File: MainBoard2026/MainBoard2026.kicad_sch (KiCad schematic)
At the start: 52 parts, among them J1 RJ25, J2 RJ25, J3 BATT_CON, J4 PRG_TWE, J5 GPS_DFROBOT_TEL-0157, J6 Micro_SD_Card_Det_Hirose_DM3AT, J7 RJ25, Q1 AO3401A, SW2 POWER, SW3 SW_Push, SW4 REG, U2 R-78E5.0-0.5, U3 MCP25625-x-SS, U4 Pico2W, U6 RX8900_mod, U7 TWE-L-WX, U8 IM920sl, Y1 16MHz

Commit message: Add files via upload
Raspberry Pi Pico W からESP32に変更　2025.09.17
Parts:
- removed D9: IM920, LED_SMD:LED_0603_1608Metric, symbol Device:LED
- removed J4: PRG_TWE, Connector_PinSocket_2.54mm:PinSocket_1x06_P2.54mm_Vertical, symbol Connector:Conn_01x06_Socket
- removed J7: RJ25, Connector_RJ:RJ25_Wayconn_MJEA-660X1_Horizontal, symbol Connector:RJ25
- removed JP2: M1, Jumper:SolderJumper-2_P1.3mm_Open_RoundedPad1.0x1.5mm, symbol Jumper:SolderJumper_2_Open
- removed JP3: BPS, Jumper:SolderJumper-2_P1.3mm_Open_RoundedPad1.0x1.5mm, symbol Jumper:SolderJumper_2_Open
- removed JP4: TX, Connector_PinHeader_2.54mm:PinHeader_1x02_P2.54mm_Vertical, symbol Jumper:SolderJumper_2_Open
- removed JP5: RX, Connector_PinHeader_2.54mm:PinHeader_1x02_P2.54mm_Vertical, symbol Jumper:SolderJumper_2_Open
- removed R12: 1k, Resistor_SMD:R_0603_1608Metric, symbol Device:R_US
- removed SW3: SW_Push, Button_Switch_SMD:SW_SPST_PTS810, symbol Switch:SW_Push
- removed SW4: REG, Button_Switch_SMD:SW_SPST_PTS810, symbol Switch:SW_Push
- removed U4: Pico2W, RPi_Pico:RPi_PicoW_SMD_TH, symbol RPi_Pico:PicoW
- removed U7: TWE-L-WX, RF_Module:MonoWireless_TWE-L-WX, symbol RF_ZigBee:TWE-L-WX
- removed U8: IM920sl, KUBTSS_parts:IM920c_ADP, symbol AKI_PARTS:IM920-DIP
- added C1, C12, C8: 0.1u, Capacitor_SMD:C_0603_1608Metric, symbol Device:C
- added C10, C11, C5: 10u, Capacitor_SMD:C_1206_3216Metric, symbol Device:C
- added C9: 1000p, Capacitor_SMD:C_0603_1608Metric, symbol Device:C
- added D11, D12: RB160M, Diode_SMD:D_SOD-123, symbol Device:D_Schottky
- added J7: USB_C_Receptacle_USB2.0_14P, Connector_USB:USB_C_Receptacle_HRO_TYPE-C-31-M-12, symbol Connector:USB_C_Receptacle_USB2.0_14P
- added Q2, Q3: MMBT3904, Package_TO_SOT_SMD:SOT-23, symbol Transistor_BJT:MMBT3904
- added R13, R14, R15, R16: 10k, Resistor_SMD:R_0603_1608Metric, symbol Device:R_US
- added R17, R18: 5.1k, Resistor_SMD:R_0603_1608Metric, symbol Device:R_US
- added SW1: RST, Button_Switch_SMD:SW_SPST_PTS810, symbol Switch:SW_Push
- added SW5: BOOT, Button_Switch_SMD:SW_SPST_PTS810, symbol Switch:SW_Push
- added U1: ESP32-WROOM-32, RF_Module:ESP32-WROOM-32, symbol RF_Module:ESP32-WROOM-32
- added U10: CH340G, Package_SO:SOIC-16_3.9x9.9mm_P1.27mm, symbol Interface_USB:CH340G
- added U9: LM1117MP-3.3, Package_TO_SOT_SMD:SOT-223-3_TabPin2, symbol Regulator_Linear:LM1117MP-3.3
- added Y2: 12MHz, Crystal:Resonator_SMD_Murata_CSTxExxV-3Pin_3.0x1.1mm, symbol Device:Resonator_Small
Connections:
- net +3V3: now also J5.1 (Pin_1), C11.1, C12.1, C5.1, C8.1, D12.2 (A), R13.1, R14.1, U1.2 (VDD), U10.16 (VCC), U10.4 (V3), U9.2 (VO)
- net +5V: no longer J5.1 (Pin_1)
- net BAT: now also U1.6 (IO34)
- net CS: now also U1.9 (IO33)
- net ERR: now also U1.7 (IO35)
- net GND: now also C1.2, C10.2, C11.2, C12.2, C5.2, C8.2, C9.2, J7.A1 (GND), J7.A12 (GND), J7.B1 (GND), J7.B12 (GND), J7.S1 (SHIELD), R17.2, R18.1, SW1.1, SW5.2, U1.1 (GND), U1.15 (GND), U1.38 (GND), U1.39 (GND), U10.1 (GND), U9.1 (GND), Y2.2
- net INT: now also U1.8 (IO32)
- net RX1: now also U1.34 (RXD0/IO3)
- net SCL: now also U1.13 (IO14)
- net SDA: now also U1.23 (IO15)
- net TX1: now also U1.35 (TXD0/IO1)
- net VSENS: now also U1.29 (IO5)
- new net: D11.2 (A), J7.A4 (VBUS), J7.A9 (VBUS), J7.B4 (VBUS), J7.B9 (VBUS)
- new net: J7.A5 (CC1), R17.1
- new net: J7.A6 (D+), J7.B6 (D+), U10.5 (UD+)
- new net: J7.A7 (D-), J7.B7 (D-), U10.6 (UD-)
- new net: J7.B5 (CC2), R18.2
- new net: Q3.1 (B), R16.2
- new net: Q2.1 (B), R15.2
- new net: C10.1, D11.1 (K), D12.1 (K), U9.3 (VI)
- new net: U10.7 (XI), Y2.1
- new net: U10.8 (XO), Y2.3
- new net DTR: Q2.2 (E), R16.1, U10.13 (~{DTR})
- new net EN: C1.1, Q2.3 (C), R13.2, SW1.2, U1.3 (EN)
- new net IO0: C9.1, Q3.3 (C), R14.2, SW5.1, U1.25 (IO0)
- new net RTS: Q3.2 (E), R15.1, U10.14 (~{RTS})
- new net RX: U1.16 (IO13), U10.2 (TXD)
- new net TX: U1.14 (IO12), U10.3 (RXD)
- no-connect marks 65 -> 25
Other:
- note added: "INPUT OUTPUT DTR RTS EN IO0 1 1 1 1 0 0 1 1 1 0 0 1 0 1 1 0"
- note removed: "Raspberry pi picoにBLE:Bluetooth Low Energyが対応している スマホとの接続、ログの管理"
- note removed: "tweliteのライターを指すためのソケット"
- note removed: "こっちのジャンパーはハンダを使うので小さい、どちらの面にあっても良い"
- note removed: "こっちはジャンパーケーブルで繋ぐ(そうすると多分ラク)ので背がある"
- note removed: "・ラズパイピコ２だけで制御と通信の両方を行えるのか ・IM920より小さい通信機でもいいな"
- moved on the sheet: C2, C3, C4, C6, D8, J6, R11, R3, U3, Y1

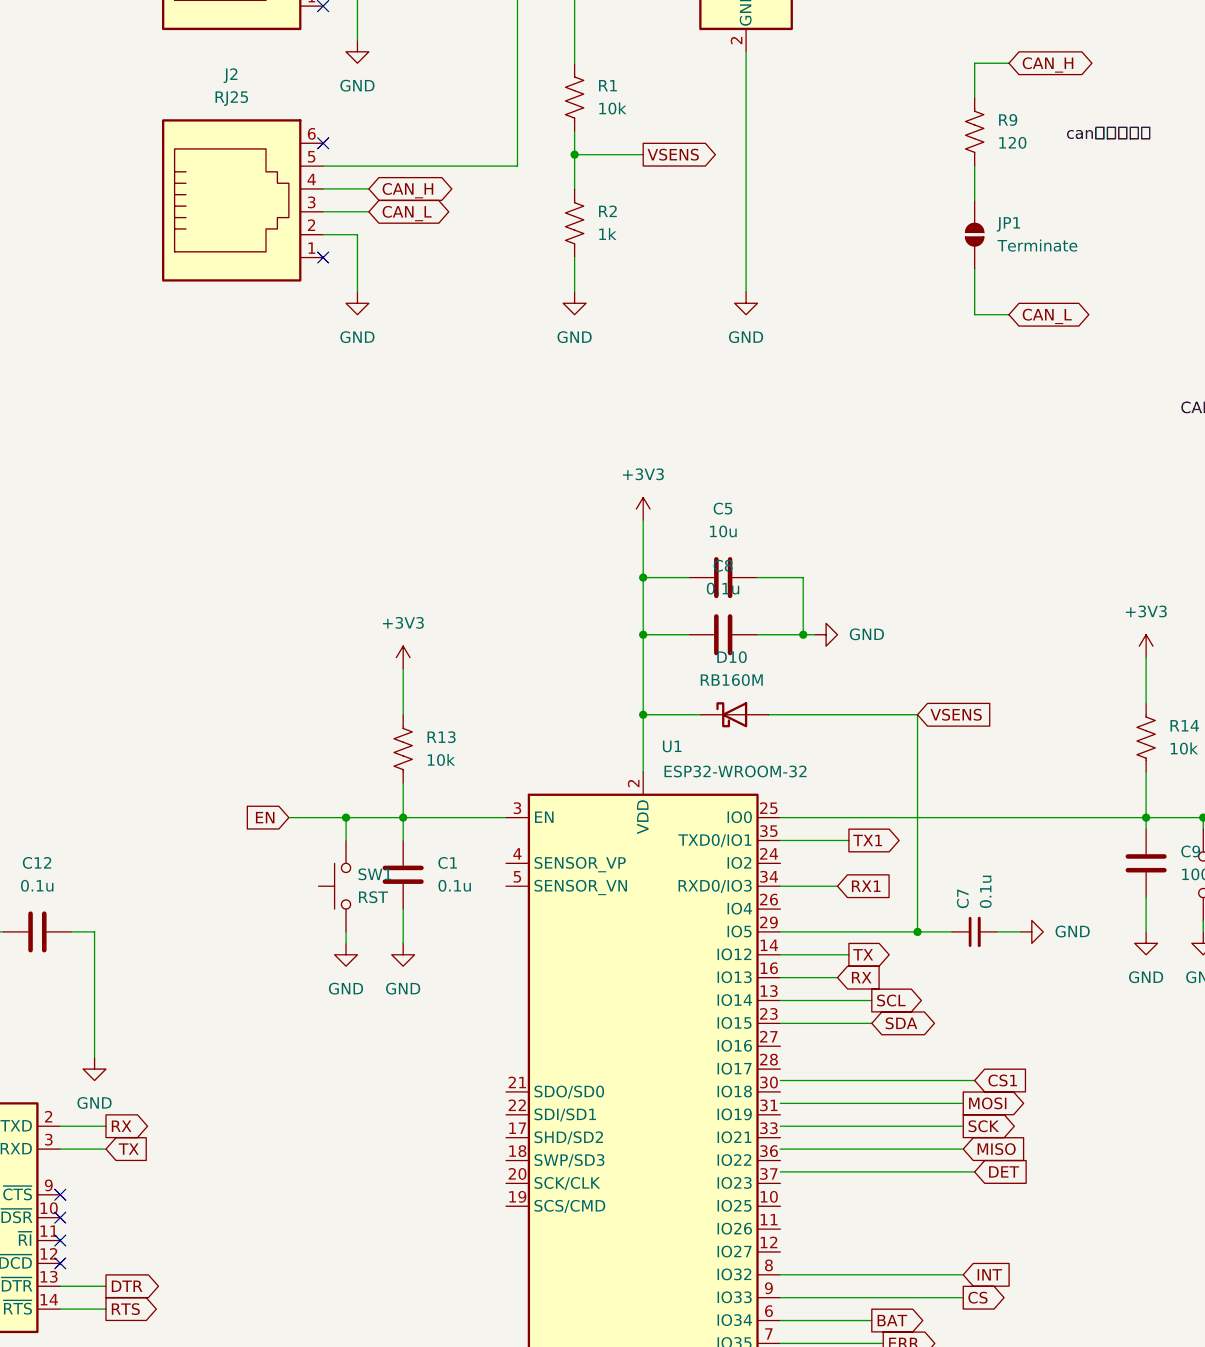
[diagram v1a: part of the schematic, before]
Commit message: Add files via upload
CANコネクタを増やした
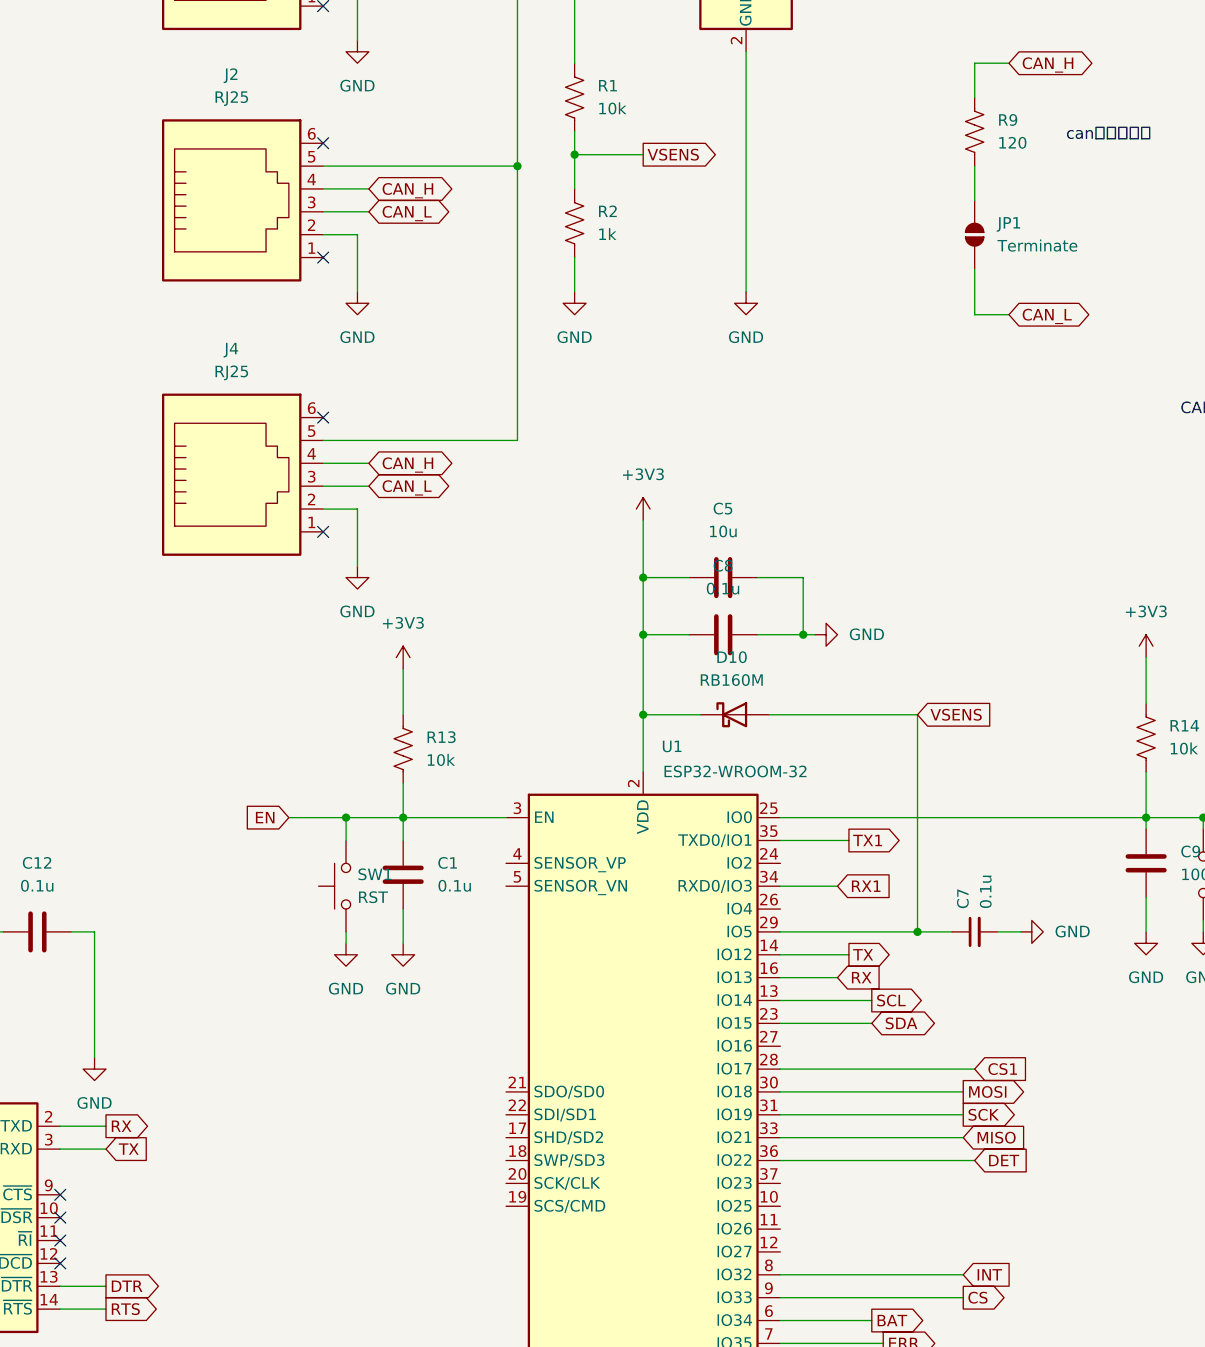
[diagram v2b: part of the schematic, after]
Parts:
- added J4: RJ25, Connector_RJ:RJ25_Wayconn_MJEA-660X1_Horizontal, symbol Connector:RJ25
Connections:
- net +BATT: now also J4.5
- net CAN_H: now also J4.4
- net CAN_L: now also J4.3
- net CS1: now also U1.28 (IO17)
- net DET: now also U1.36 (IO22)
- net GND: now also J4.2
- net MISO: now also U1.33 (IO21)
- net MOSI: now also U1.30 (IO18)
- net SCK: now also U1.31 (IO19)
- no-connect marks 25 -> 27

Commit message: Add files via upload
試作前完成版
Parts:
- removed D2: Zener_12V, Diode_SMD:D_SOD-323, symbol Device:D_Zener
- removed D3: MA10EB045, Diode_SMD:Vishay_SMPA, symbol Device:D_Schottky
- removed J3: BATT_CON, Connector_AMASS:AMASS_XT60PW-M_1x02_P7.20mm_Horizontal, symbol Connector_Generic:Conn_01x02
- removed Q1: AO3401A, Package_TO_SOT_SMD:SOT-23, symbol Device:Q_PMOS_GDS
- removed R4: 10k, Resistor_SMD:R_0603_1608Metric, symbol Device:R_US
- removed R8: 100, Resistor_SMD:R_0603_1608Metric, symbol Device:R_US
- removed SW2: POWER, KUBTSS:toggle, symbol Switch:SW_SPDT
- added C13: 10u, Capacitor_SMD:C_0603_1608Metric, symbol Device:C_Small
- added C14, C16, C21, C23, C24, C27, C28: 0.1u, Capacitor_SMD:C_0603_1608Metric, symbol Device:C_Small
- added C15: 1u, Capacitor_SMD:C_0603_1608Metric, symbol Device:C_Small
- added C17: 100u, Capacitor_SMD:C_1206_3216Metric, symbol Device:C
- added C18: 1n, Capacitor_SMD:C_1206_3216Metric, symbol Device:C
- added C19, C20: 0.1u, Capacitor_SMD:C_0603_1608Metric, symbol Device:C
- added C22, C25, C26, C29: 22u, Capacitor_SMD:C_0603_1608Metric, symbol Device:C_Small
- added D20: Zener_10V, Diode_SMD:D_SOD-323, symbol Device:D_Zener
- added D9: RB160M, Diode_SMD:D_SOD-123, symbol Device:D_Schottky
- added F1, F2: Fuse, symbol Device:Fuse
- added FB1: FerriteBead_Small, symbol Device:FerriteBead_Small
- added J8: BATT_CON, Connector_AMASS:AMASS_XT60PW-M_1x02_P7.20mm_Horizontal, symbol Connector_Generic:Conn_01x02
- added Q4: AO3401A, Package_TO_SOT_SMD:SOT-23, symbol Device:Q_PMOS_GDS
- added R12, R19, R23, R25, R27, R42: 100k, Resistor_SMD:R_0603_1608Metric, symbol Device:R_US
- added R20, R21, R22: 47, Resistor_SMD:R_0603_1608Metric, symbol Device:R_US
- added R24, R40, R44: 100, Resistor_SMD:R_0603_1608Metric, symbol Device:R_US
- added R26: 200k, Resistor_SMD:R_0603_1608Metric, symbol Device:R_US
- added R28, R29: 2.2k, Resistor_SMD:R_0603_1608Metric, symbol Device:R_US
- added R30, R31, R32, R33: 33, Resistor_SMD:R_0603_1608Metric, symbol Device:R_US
- added R34, R35: 0.3, Resistor_SMD:R_0603_1608Metric, symbol Device:R_US
- added R36, R37: 22, Resistor_SMD:R_0603_1608Metric, symbol Device:R_US
- added R38: 3.3k, Resistor_SMD:R_0603_1608Metric, symbol Device:R_US
- added R39: 6.8k, Resistor_SMD:R_0603_1608Metric, symbol Device:R_US
- added R41: 1M, Resistor_SMD:R_0603_1608Metric, symbol Device:R_US
- added SW3: POWER, KUBTSS:toggle, symbol Switch:SW_SPDT
- added U4: R-78E3.3-0.5, Converter_DCDC:Converter_DCDC_RECOM_R-78E-0.5_THT, symbol Regulator_Switching:R-78E5.0-0.5
- C1: value 0.1u -> 0.47u
- C2: value 0.1u -> 10u
- C3: value 0.1u -> 1u
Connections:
- net +3V3: now also C13.2, C15.1, C16.1, C17.1, R12.2, R19.2, R28.1, R29.1; no longer C2.2, C3.1, U10.16 (VCC), U10.4 (V3), U3.19 (VDD)
- net +5V: now also C3.1, U3.19 (VDD), C14.1, C22.2, C23.2, FB1.1; no longer C4.1, U3.27 (VDDA)
- net +BATT: now also C24.2, C25.2, C26.2, C27.2, D9.1 (K), Q4.2 (D), U4.1 (IN)
- net CS1: now also R21.1, R30.2; no longer J6.2 (DAT3/CD), U1.28 (IO17)
- net GND: now also C2.2, J6.11 (SHIELD), C13.1, C14.2, C15.2, C16.2, C17.2, C18.2, C19.2, C22.1, C23.1, C24.1, C25.1, C26.1, C27.1, C28.1, C29.1, J8.1 (Pin_1), R23.2, R25.2, R34.2, R35.1, R39.2, R41.2, SW3.1 (A), U4.2 (GND); no longer C10.2, C11.2, C2.1, J7.S1 (SHIELD), U3.5 (STBY)
- net IO0: now also R24.2; no longer U1.25 (IO0)
- net MISO: now also R33.2; no longer U1.33 (IO21)
- net MOSI: now also R22.1, R31.2; no longer J6.3 (CMD), U1.30 (IO18)
- net RX: now also R38.1, R39.1; no longer U10.2 (TXD)
- net SCK: now also R20.1, R32.2; no longer D4.2 (A), D8.2 (A), J6.5 (CLK), U1.31 (IO19)
- net SCL: now also R28.2
- net SDA: now also R29.2
- net TX: now also R25.1, R40.1; no longer U10.3 (RXD)
- net VSENS: now also R26.2, R27.1; no longer C7.1, D10.2 (A), U1.29 (IO5)
- net at J7.A4 (VBUS), J7.A9 (VBUS), J7.B4 (VBUS)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: now also F1.2; no longer D11.2 (A)
- net at J7.A6 (D+), J7.B6 (D+): now also R37.2; no longer U10.5 (UD+)
- net at J7.A7 (D-), J7.B7 (D-): now also R36.2; no longer U10.6 (UD-)
- net at C10.1, D11.1 (K), D12.1 (K)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: now also C20.1
- net LED1: now reaches U1.10 (IO25)
- net LED1: now also D4.2 (A)
- net LED2: now reaches U1.11 (IO26)
- net LED2: now also D8.2 (A)
- net at J6.1 (DAT2): now also J6.8 (DAT1), R19.1
- new net: R24.1, U1.25 (IO0)
- new net: J6.2 (DAT3/CD), R12.1, R21.2
- new net: R36.1, U10.6 (UD-)
- new net: C18.1, J7.S1 (SHIELD), R41.1
- new net: R23.1, U3.5 (STBY)
- new net: R42.1, R44.1, SW3.2 (B)
- new net: C21.2, D20.1 (K), F2.2, Q4.3 (S), R42.2, SW3.3 (C)
- new net: C7.1, R27.2, U1.29 (IO5)
- new net: R40.2, U10.3 (RXD)
- new net: C11.2, R35.2
- new net: C10.2, R34.1
- new net: R37.1, U10.5 (UD+)
- new net: C2.1, C4.1, FB1.2, U3.27 (VDDA)
- new net: C19.1, U10.4 (V3)
- new net: C21.1, D20.2 (A), Q4.1 (G), R44.2
- new net: J6.3 (CMD), R22.2
- new net: R31.1, U1.30 (IO18)
- new net: J6.5 (CLK), R20.2
- new net: D10.2 (A), R26.1
- new net: R30.1, U1.28 (IO17)
- new net: R32.1, U1.31 (IO19)
- new net: R33.1, U1.33 (IO21)
- new net: F2.1, J8.2 (Pin_2)
- new net: C20.2, U10.16 (VCC)
- new net: R38.2, U10.2 (TXD)
- new net: D11.2 (A), F1.1
- new net +3.3V: C28.2, C29.2, D9.2 (A), U4.3 (OUT)
- no-connect marks 27 -> 24
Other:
- note added: "D"
- note added: "G"
- note added: "S"
- note added: "VDD近くに配置"
- moved on the sheet: C1, C10, C11, C12, C3, C4, C5, C6, C7, C8, C9, D1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

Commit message: Add files via upload
試作後　抵抗値など修正　2025.10.25
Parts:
- removed R22: 47, Resistor_SMD:R_0603_1608Metric, symbol Device:R_US
- removed R33: 33, Resistor_SMD:R_0603_1608Metric, symbol Device:R_US
- added R4: 100k, Resistor_SMD:R_0603_1608Metric, symbol Device:R_US
- added R8: 22, Resistor_SMD:R_0603_1608Metric, symbol Device:R_US
- C21: value 0.1u -> 1u
- R12: value 100k -> 47k
- R20: value 47 -> 22
- R21: value 47 -> 33
- R44: value 100 -> 4.7k
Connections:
- net +3V3: now also R4.1
- net +BATT: no longer Q4.2 (D)
- net CS: now also R20.2, R21.1; no longer U1.9 (IO33), U3.17 (~{CS})
- net CS1: now also J6.2 (DAT3/CD), R12.1; no longer R21.1
- net GND: now also C20.1
- net MISO: now also U1.33 (IO21), R8.2; no longer J6.7 (DAT0)
- net MOSI: now also J6.3 (CMD), R4.2
- net RX: now also U1.34 (RXD0/IO3); no longer U1.16 (IO13)
- net RX1: now also U1.16 (IO13); no longer U1.34 (RXD0/IO3)
- net SCK: now also J6.5 (CLK); no longer R20.1
- net TX: now also U1.35 (TXD0/IO1); no longer R25.1, U1.14 (IO12)
- net TX1: now also R25.1, U1.14 (IO12); no longer U1.35 (TXD0/IO1)
- net at C10.1, D11.1 (K), D12.1 (K)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: now also C20.2, U10.16 (VCC); no longer C20.1
- new net: R20.1, U3.17 (~{CS})
- new net: R21.2, U1.9 (IO33)
- new net: J6.7 (DAT0), R8.1
- new net +out: Q4.2 (D)
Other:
- note added: "SdFat.h"
- moved on the sheet: C10, C11, C12, C18, C19, C20, D11, D12, F1, J7, Q2, Q3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

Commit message: Add files via upload
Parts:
- removed R28, R29: 2.2k, Resistor_SMD:R_0603_1608Metric, symbol Device:R_US
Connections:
- net +3V3: no longer J5.1 (Pin_1)
- net +5V: now also J5.1 (Pin_1)
- net RX1: now also U1.27 (IO16); no longer U1.16 (IO13)
- net TX1: now also U1.12 (IO27); no longer R25.1, U1.14 (IO12)
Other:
- moved on the sheet: R25

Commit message: Add files via upload
フットプリント設定完了
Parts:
- removed C1: 0.47u, Capacitor_SMD:C_0603_1608Metric, symbol Device:C
- removed C10, C11: 10u, Capacitor_SMD:C_1206_3216Metric, symbol Device:C
- removed C12, C19, C20: 0.1u, Capacitor_SMD:C_0603_1608Metric, symbol Device:C
- removed C18: 1n, Capacitor_SMD:C_1206_3216Metric, symbol Device:C
- removed C9: 1000p, Capacitor_SMD:C_0603_1608Metric, symbol Device:C
- removed D11, D12: RB160M, Diode_SMD:D_SOD-123, symbol Device:D_Schottky
- removed F1: Fuse, symbol Device:Fuse
- removed J7: USB_C_Receptacle_USB2.0_14P, Connector_USB:USB_C_Receptacle_HRO_TYPE-C-31-M-12, symbol Connector:USB_C_Receptacle_USB2.0_14P
- removed Q2, Q3: MMBT3904, Package_TO_SOT_SMD:SOT-23, symbol Transistor_BJT:MMBT3904
- removed R13, R14, R15, R16: 10k, Resistor_SMD:R_0603_1608Metric, symbol Device:R_US
- removed R17, R18: 5.1k, Resistor_SMD:R_0603_1608Metric, symbol Device:R_US
- removed R24, R40: 100, Resistor_SMD:R_0603_1608Metric, symbol Device:R_US
- removed R34, R35: 0.3, Resistor_SMD:R_0603_1608Metric, symbol Device:R_US
- removed R36, R37: 22, Resistor_SMD:R_0603_1608Metric, symbol Device:R_US
- removed R38: 3.3k, Resistor_SMD:R_0603_1608Metric, symbol Device:R_US
- removed R39: 6.8k, Resistor_SMD:R_0603_1608Metric, symbol Device:R_US
- removed R41: 1M, Resistor_SMD:R_0603_1608Metric, symbol Device:R_US
- removed SW1: RST, Button_Switch_SMD:SW_SPST_PTS810, symbol Switch:SW_Push
- removed SW5: BOOT, Button_Switch_SMD:SW_SPST_PTS810, symbol Switch:SW_Push
- removed U10: CH340G, Package_SO:SOIC-16_3.9x9.9mm_P1.27mm, symbol Interface_USB:CH340G
- removed U9: LM1117MP-3.3, Package_TO_SOT_SMD:SOT-223-3_TabPin2, symbol Regulator_Linear:LM1117MP-3.3
- removed Y2: 12MHz, Crystal:Resonator_SMD_Murata_CSTxExxV-3Pin_3.0x1.1mm, symbol Device:Resonator_Small
- F2: value Fuse -> MF-R090; footprint (none) -> KUBTSS:Fuse MF-R090
- FB1: footprint (none) -> Inductor_SMD:L_0603_1608Metric
- U5: footprint KUBTSS_parts:Gyro_AE-BNO055-BO -> KUBTSS:BNO055
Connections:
- net IO0: now also U1.25 (IO0)
- no-connect marks 24 -> 19
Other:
- note removed: "INPUT OUTPUT DTR RTS EN IO0 1 1 1 1 0 0 1 1 1 0 0 1 0 1 1 0"
